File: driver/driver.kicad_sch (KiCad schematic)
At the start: 0 parts

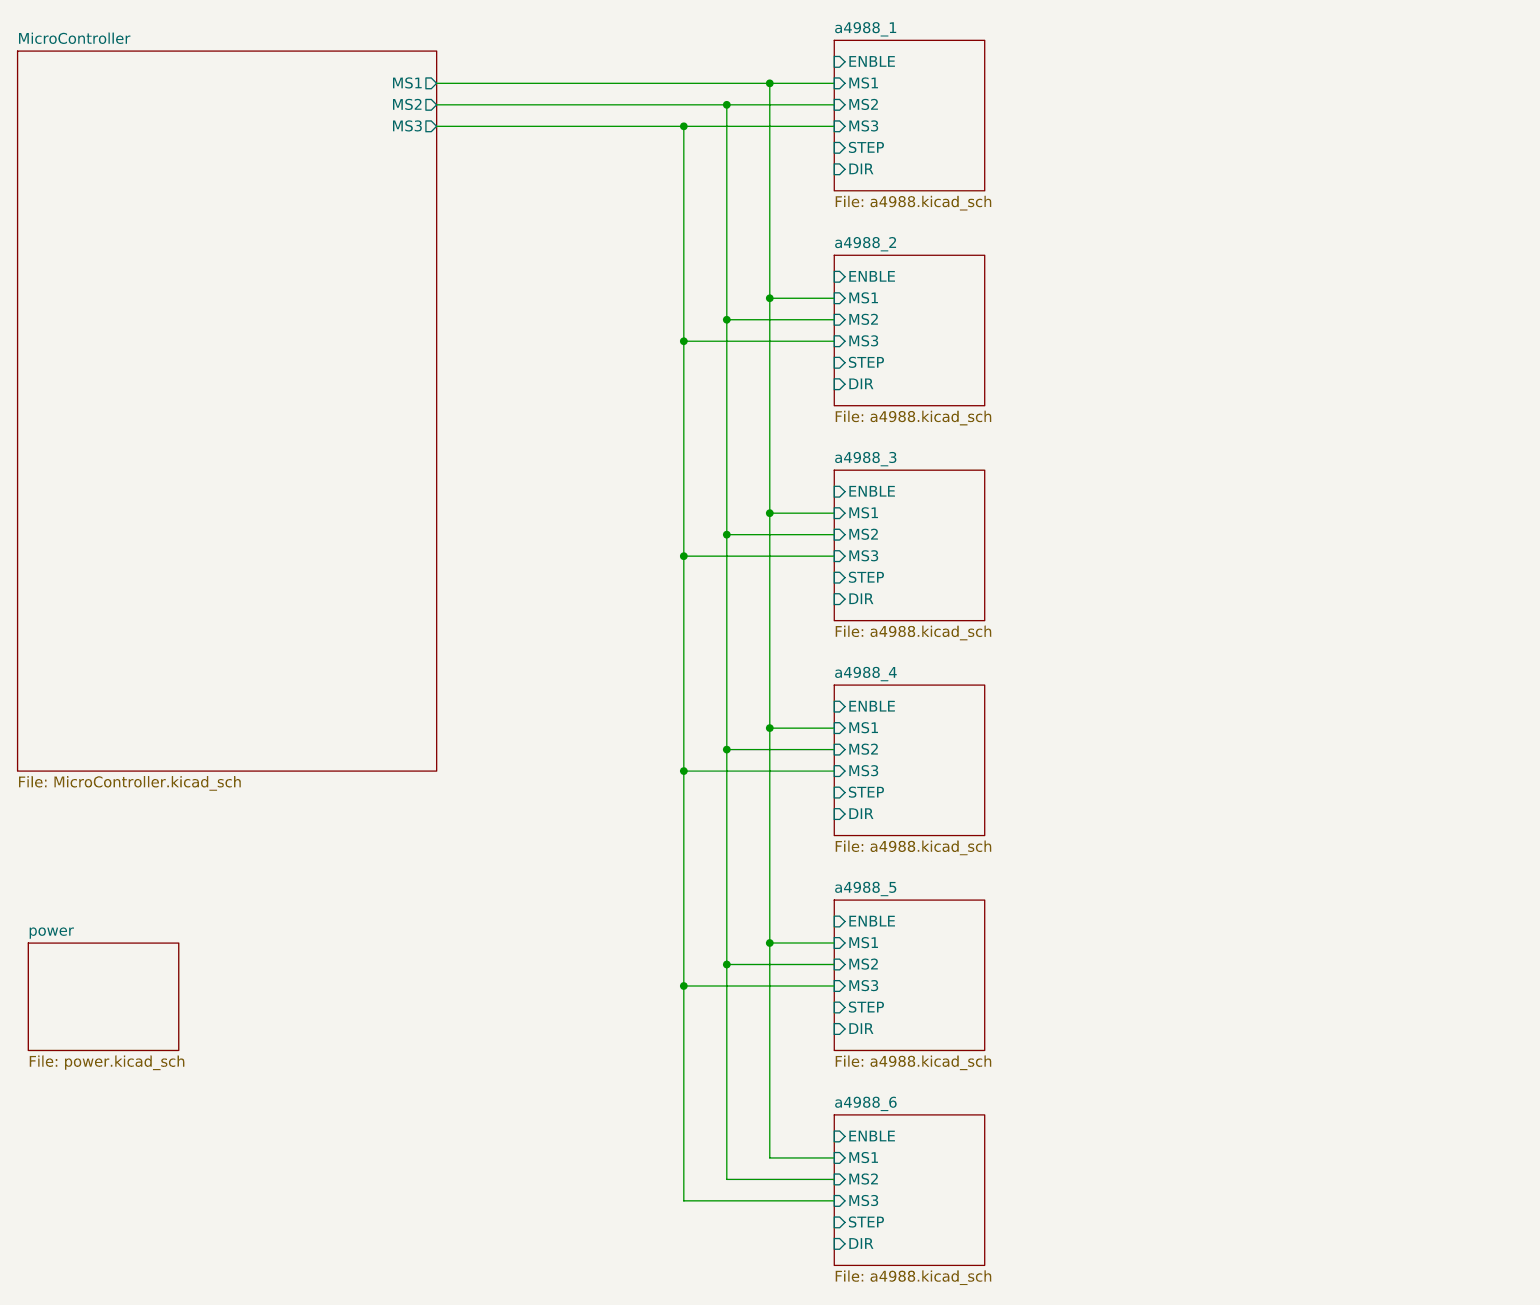
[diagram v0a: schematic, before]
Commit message: 部品配置完了
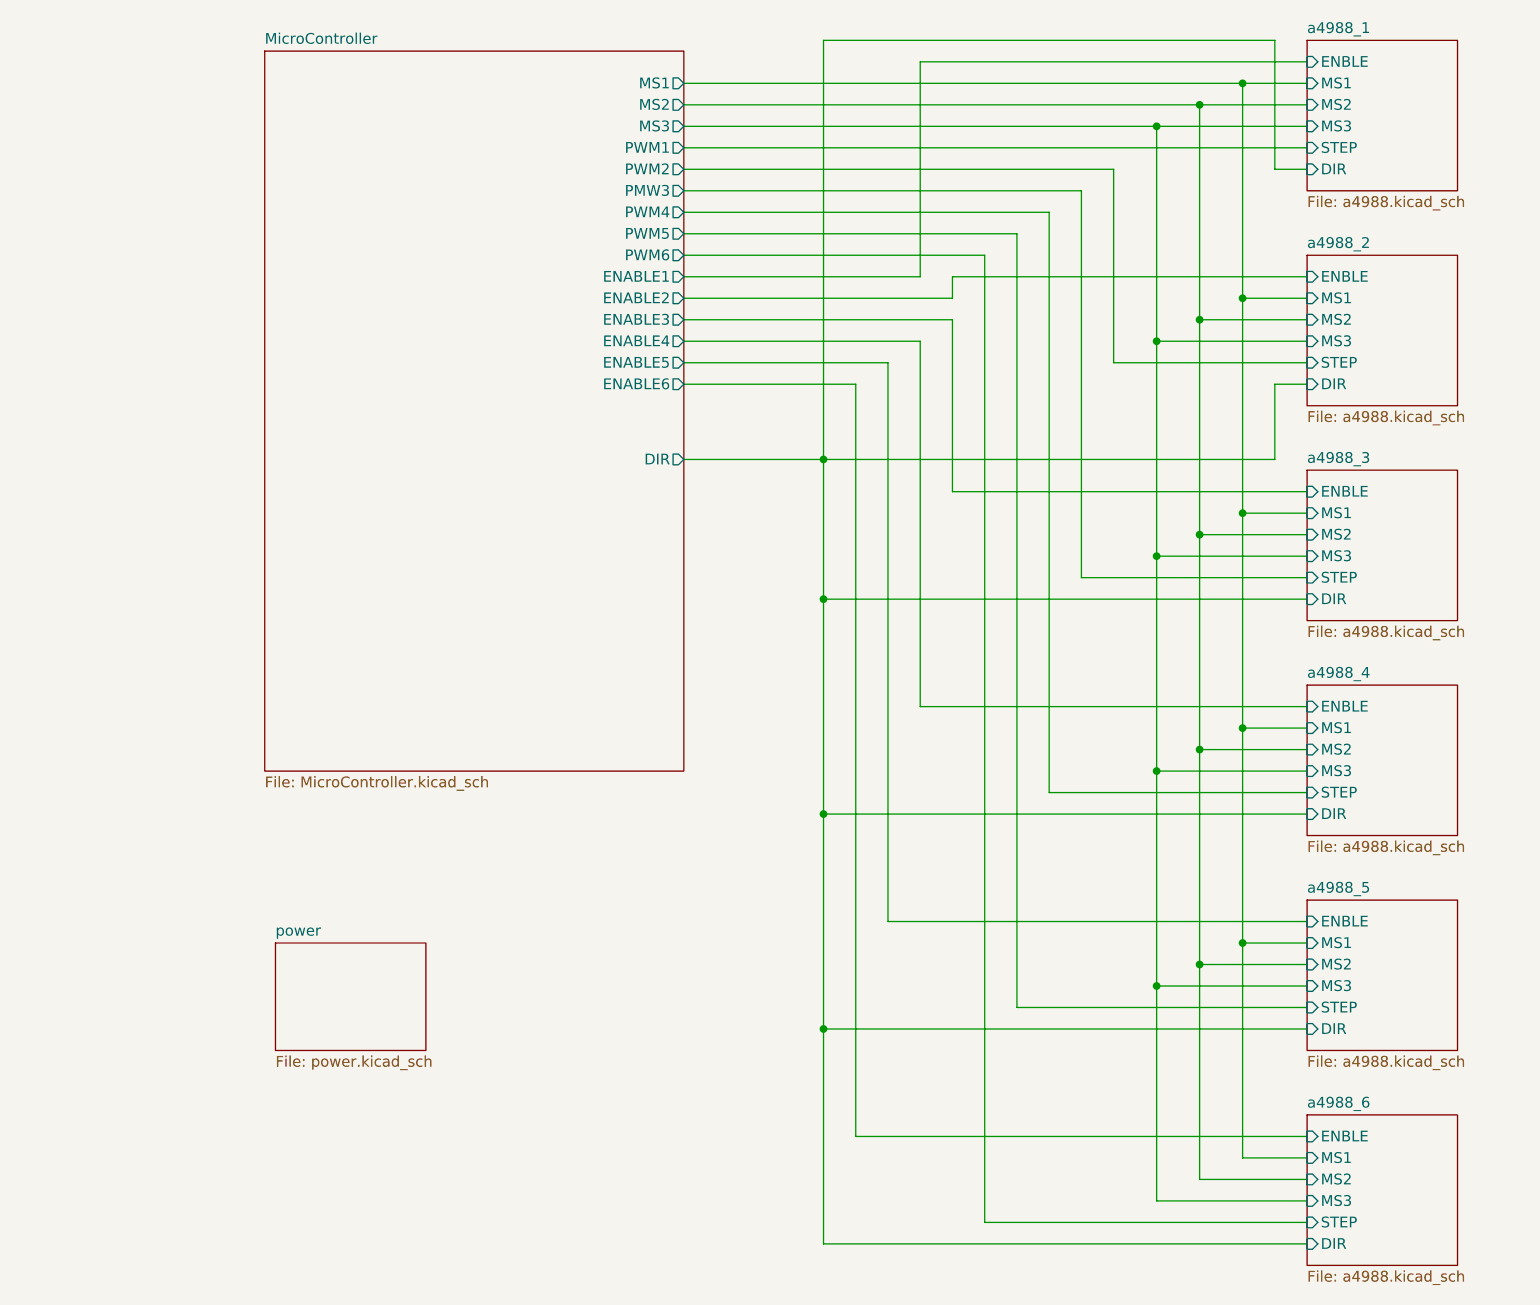
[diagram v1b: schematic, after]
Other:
- sheet MicroController ports: added DIR, ENABLE1, ENABLE2, ENABLE3, ENABLE4, ENABLE5, ENABLE6, PMW3, PWM1, PWM2, PWM4, PWM5, PWM6; removed none
